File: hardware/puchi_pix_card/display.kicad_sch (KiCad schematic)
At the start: 286 parts, among them Q101 AO3401A, Q102 AO3401A, Q103 AO3401A, Q104 AO3401A, Q105 AO3401A, Q106 AO3401A, Q107 AO3401A, Q108 AO3401A, Q109 AO3401A, Q110 AO3401A, Q111 AO3401A, Q112 AO3401A, Q113 AO3401A, Q114 AO3401A, Q115 AO3401A, Q116 AO3401A, U101 MBI5153GP (R), U102 MBI5153GP (G), U103 MBI5153GP (B), U104 74HCT595, U105 74HCT595

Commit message: Fix design-review findings: I2C/PFET-gate pull-ups, red-column VDROP, D1/L1 part selection, USB-C 16P, USB power policy, MBI GCLK dead time and sleep leak paths
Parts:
- added R105, R106, R107, R108, R109, R110, R111, R112, R113, R114, R115, R116, R117, R118, R119, R120: 180, Resistor_SMD:R_0402_1005Metric, symbol Device:R
- added R121, R122, R123, R124, R125, R126, R127, R128, R129, R130, R131, R132, R133, R134, R135, R136: 100k, Resistor_SMD:R_0402_1005Metric, symbol Device:R
- R101: value 1.5k -> 1.8k
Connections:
- net +5V: now also R121.1, R122.1, R123.1, R124.1, R125.1, R126.1, R127.1, R128.1, R129.1, R130.1, R131.1, R132.1, R133.1, R134.1, R135.1, R136.1
- net COL_R0: now also R105.2; no longer U101.5 (OUT0)
- net COL_R1: now also R106.2; no longer U101.6 (OUT1)
- net COL_R10: now also R115.2; no longer U101.15 (OUT10)
- net COL_R11: now also R116.2; no longer U101.16 (OUT11)
- net COL_R12: now also R117.2; no longer U101.17 (OUT12)
- net COL_R13: now also R118.2; no longer U101.18 (OUT13)
- net COL_R14: now also R119.2; no longer U101.19 (OUT14)
- net COL_R15: now also R120.2; no longer U101.20 (OUT15)
- net COL_R2: now also R107.2; no longer U101.7 (OUT2)
- net COL_R3: now also R108.2; no longer U101.8 (OUT3)
- net COL_R4: now also R109.2; no longer U101.9 (OUT4)
- net COL_R5: now also R110.2; no longer U101.10 (OUT5)
- net COL_R6: now also R111.2; no longer U101.11 (OUT6)
- net COL_R7: now also R112.2; no longer U101.12 (OUT7)
- net COL_R8: now also R113.2; no longer U101.13 (OUT8)
- net COL_R9: now also R114.2; no longer U101.14 (OUT9)
- net SR_Q0: now also R121.2
- net SR_Q1: now also R122.2
- net SR_Q10: now also R131.2
- net SR_Q11: now also R132.2
- net SR_Q12: now also R133.2
- net SR_Q13: now also R134.2
- net SR_Q14: now also R135.2
- net SR_Q15: now also R136.2
- net SR_Q2: now also R123.2
- net SR_Q3: now also R124.2
- net SR_Q4: now also R125.2
- net SR_Q5: now also R126.2
- net SR_Q6: now also R127.2
- net SR_Q7: now also R128.2
- net SR_Q8: now also R129.2
- net SR_Q9: now also R130.2
- new net: R105.1, U101.5 (OUT0)
- new net: R108.1, U101.8 (OUT3)
- new net: R120.1, U101.20 (OUT15)
- new net: R113.1, U101.13 (OUT8)
- new net: R109.1, U101.9 (OUT4)
- new net: R117.1, U101.17 (OUT12)
- new net: R110.1, U101.10 (OUT5)
- new net: R114.1, U101.14 (OUT9)
- new net: R111.1, U101.11 (OUT6)
- new net: R112.1, U101.12 (OUT7)
- new net: R115.1, U101.15 (OUT10)
- new net: R116.1, U101.16 (OUT11)
- new net: R118.1, U101.18 (OUT13)
- new net: R119.1, U101.19 (OUT14)
- new net: R106.1, U101.6 (OUT1)
- new net: R107.1, U101.7 (OUT2)
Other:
- note added: "Rext: IOUT=(0.61V/Rext)x24 (MBI5153 p21) -> R 1.8k=8.1mA (+180R series drop, MBI DS p24), G 2.4k=6.1mA, B 4.7k=3.1mA max; config gain 12.5-200%."
- note removed: "Rext: IOUT=(0.61V/Rext)x24 (MBI5153 p21) -> R 1.5k=9.8mA, G 2.4k=6.1mA, B 4.7k=3.1mA max; config gain 12.5-200%."

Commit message: Fill LCSC part numbers for JLCPCB assembly; switch the column drivers to MBI5124GP-B (pin 21 GCLK -> /OE, net MBI_OE); R2 133k, in-stock LED/NOR listings
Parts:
- C101, C102, C103, C104, C105: LCSC (none) -> C309458
- D101, D102, D103, D104, D105, D106, D107, D108, D109, D110, D111, D112, D113, D114, D115, D116, D117, D118, D119, D120, D121, D122, D123, D124, D125, D126, D127, D128, D129, D130, D131, D132, D133, D134, D135, D136, D137, D138, D139, D140, D141, D142, D143, D144, D145, D146, D147, D148, D149, D150, D151, D152, D153, D154, D155, D156, D157, D158, D159, D160, D161, D162, D163, D164, D165, D166, D167, D168, D169, D170, D171, D172, D173, D174, D175, D176, D177, D178, D179, D180, D181, D182, D183, D184, D185, D186, D187, D188, D189, D190, D191, D192, D193, D194, D195, D196, D197, D198, D199, D200, D201, D202, D203, D204, D205, D206, D207, D208, D209, D210, D211, D212, D213, D214, D215, D216, D217, D218, D219, D220, D221, D222, D223, D224, D225, D226, D227, D228, D229, D230, D231, D232, D233, D234, D235, D236, D237, D238, D239, D240, D241, D242, D243, D244, D245, D246, D247, D248, D249, D250, D251, D252, D253, D254, D255, D256, D257, D258, D259, D260, D261, D262, D263, D264, D265, D266, D267, D268, D269, D270, D271, D272, D273, D274, D275, D276, D277, D278, D279, D280, D281, D282, D283, D284, D285, D286, D287, D288, D289, D290, D291, D292, D293, D294, D295, D296, D297, D298, D299, D300, D301, D302, D303, D304, D305, D306, D307, D308, D309, D310, D311, D312, D313, D314, D315, D316, D317, D318, D319, D320, D321, D322, D323, D324, D325, D326, D327, D328, D329, D330, D331, D332, D333, D334, D335, D336, D337, D338, D339, D340, D341, D342, D343, D344, D345, D346, D347, D348, D349, D350, D351, D352, D353, D354, D355, D356: LCSC C108793 -> C42421005
- Q101, Q102, Q103, Q104, Q105, Q106, Q107, Q108, Q109, Q110, Q111, Q112, Q113, Q114, Q115, Q116: LCSC (none) -> C15127
- R101: LCSC (none) -> C25871
- R102: LCSC (none) -> C25882
- R103: LCSC (none) -> C25900
- R104: LCSC (none) -> C25744
- R105, R106, R107, R108, R109, R110, R111, R112, R113, R114, R115, R116, R117, R118, R119, R120: LCSC (none) -> C38941
- R121, R122, R123, R124, R125, R126, R127, R128, R129, R130, R131, R132, R133, R134, R135, R136: LCSC (none) -> C25741
- U101: value MBI5153GP (R) -> MBI5124GP-B (R); symbol puchi_pix_card:MBI5153GP -> puchi_pix_card:MBI5124GP; LCSC C183654 -> C256866
- U102: value MBI5153GP (G) -> MBI5124GP-B (G); symbol puchi_pix_card:MBI5153GP -> puchi_pix_card:MBI5124GP; LCSC C183654 -> C256866
- U103: value MBI5153GP (B) -> MBI5124GP-B (B); symbol puchi_pix_card:MBI5153GP -> puchi_pix_card:MBI5124GP; LCSC C183654 -> C256866
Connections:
- net GCLK renamed MBI_OE

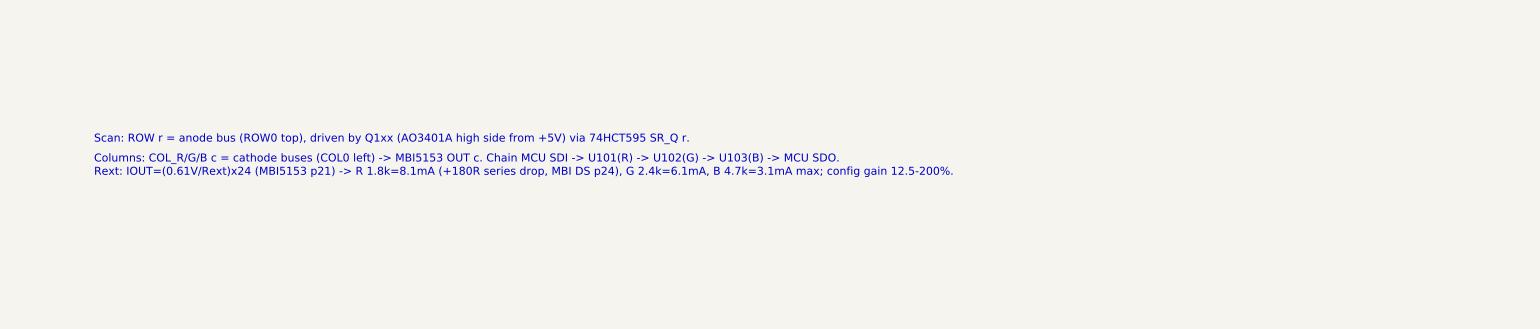
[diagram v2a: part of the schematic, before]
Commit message: Review fixes: guard the first plane against ISR re-entry, SPI2 8 MHz for the 3.3V chain delay, release the KXTJ3 latched INT, force /OE high on stop; J2 real part name and footprint id; drop MBI5153 leftovers
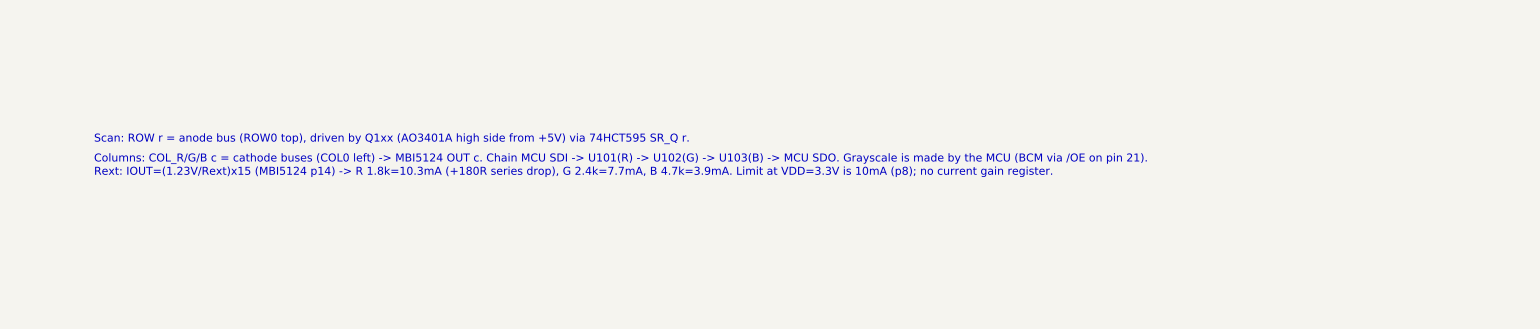
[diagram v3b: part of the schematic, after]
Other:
- note added: "Columns: COL_R/G/B c = cathode buses (COL0 left) -> MBI5124 OUT c. Chain MCU SDI -> U101(R) -> U102(G) -> U103(B) -> MCU SDO. Grayscale is made by the MCU (BCM via /OE on pin 21)."
- note added: "Rext: IOUT=(1.23V/Rext)x15 (MBI5124 p14) -> R 1.8k=10.3mA (+180R series drop), G 2.4k=7.7mA, B 4.7k=3.9mA. Limit at VDD=3.3V is 10mA (p8); no current gain register."
- note removed: "Columns: COL_R/G/B c = cathode buses (COL0 left) -> MBI5153 OUT c. Chain MCU SDI -> U101(R) -> U102(G) -> U103(B) -> MCU SDO."
- note removed: "Rext: IOUT=(0.61V/Rext)x24 (MBI5153 p21) -> R 1.8k=8.1mA (+180R series drop, MBI DS p24), G 2.4k=6.1mA, B 4.7k=3.1mA max; config gain 12.5-200%."
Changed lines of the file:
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@@
 		)
 	)
-	(text "Columns: COL_R/G/B c = cathode buses (COL0 left) -> MBI5153 OUT c. Chain MCU SDI -> U101(R) -> U102(G) -> U103(B) -> MCU SDO."
+	(text "Columns: COL_R/G/B c = cathode buses (COL0 left) -> MBI5124 OUT c. Chain MCU SDI -> U101(R) -> U102(G) -> U103(B) -> MCU SDO. Grayscale is made by the MCU (BCM via /OE on pin 21)."
 		(exclude_from_sim no)
 		(at 299.72 303.53 0)
@@
 		)
 	)
-	(text "Rext: IOUT=(0.61V/Rext)x24 (MBI5153 p21) -> R 1.8k=8.1mA (+180R series drop, MBI DS p24), G 2.4k=6.1mA, B 4.7k=3.1mA max; config gain 12.5-200%."
+	(text "Rext: IOUT=(1.23V/Rext)x15 (MBI5124 p14) -> R 1.8k=10.3mA (+180R series drop), G 2.4k=7.7mA, B 4.7k=3.9mA. Limit at VDD=3.3V is 10mA (p8); no current gain register."
 		(exclude_from_sim no)
 		(at 299.72 306.07 0)

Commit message: Move SW1 into the +3V3S branch (boost VIN on VBAT) so the 0.1A switch carries only the MCU rail; R101 2.0k / red series 120R for the MBI5124 10mA limit and USB headroom; R9 4.7k; C1 next to U1; In1 GND plane rejoined
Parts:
- R101: value 1.8k -> 2.0k; LCSC C25871 -> C4109
- R105, R106, R107, R108, R109, R110, R111, R112, R113, R114, R115, R116, R117, R118, R119, R120: value 180 -> 120; LCSC C38941 -> C25079
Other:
- note added: "Rext: IOUT=(1.23V/Rext)x15 (MBI5124 p14) -> R 2.0k=9.2mA (+120R series drop), G 2.4k=7.7mA, B 4.7k=3.9mA. Limit at VDD=3.3V is 10mA (p8); no current gain register. Red series 120R: on USB (+5V >= 4.0V after D1) worst-case red VF 2.4V + 1.11V + VDS 0.5V = 4.0V."
- note removed: "Rext: IOUT=(1.23V/Rext)x15 (MBI5124 p14) -> R 1.8k=10.3mA (+180R series drop), G 2.4k=7.7mA, B 4.7k=3.9mA. Limit at VDD=3.3V is 10mA (p8); no current gain register."

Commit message: Add C106 10uF bulk capacitor on +5V next to the row PFET column (row switching transient, USB headroom)
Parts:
- added C106: 10uF, Capacitor_SMD:C_0603_1608Metric, symbol Device:C
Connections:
- net +5V: now also C106.1
- net GND: now also C106.2
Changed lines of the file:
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@@
 	(wire
 		(pts
+			(xy 474.98 109.22) (xy 474.98 106.68)
+		)
+		(stroke
+			(width 0)
+			(type default)
+		)
+	)
+	(global_label "+5V"
+		(shape input)
+		(at 474.98 106.68 90)
+		(effects
+			(font
+				(size 1.27 1.27)
+			)
+			(justify left)
+		)
+		(property "Intersheetrefs" "${INTERSHEET_REFS}"
+			(at 535.94 157.48 0)
+			(effects
+				(font
+					(size 1.27 1.27)
+				)
+				(hide yes)
+			)
+		)
+	)
+	(wire
+		(pts
 			(xy 269.24 95.25) (xy 269.24 97.79)
 		)
@@
 					(unit 1)
 				)
+			)
+		)
+	)
+	(symbol
+		(lib_id "Device:C")
+		(at 474.98 113.03 0)
+		(unit 1)
+		(exclude_from_sim no)
+		(in_bom yes)
+		(on_board yes)
+		(dnp no)
+		(property "Reference" "C106"
+			(at 477.52 111.76 0)
+			(effects
+				(font
+					(size 1.27 1.27)
+				)
+				(justify left)
+			)
+		)
+		(property "Value" "10uF"
+			(at 477.52 114.3 0)
+			(effects
+				(font
+					(size 1.016 1.016)
+				)
+				(justify left)
+			)
+		)
+		(property "Footprint" "Capacitor_SMD:C_0603_1608Metric"
+			(at 474.98 113.03 0)
+			(effects
+				(font
+					(size 1.27 1.27)
+				)
+				(hide yes)
+			)
+		)
+		(property "Datasheet" ""
+			(at 474.98 113.03 0)
+			(effects
+				(font
+					(size 1.27 1.27)
+				)
+				(hide yes)
+			)
+		)
+		(property "Description" ""
+			(at 474.98 113.03 0)
+			(effects
+				(font
+					(size 1.27 1.27)
+				)
+			)
+		)
+		(property "LCSC" "C96446"
+			(at 474.98 113.03 0)
+			(effects
+				(font
+					(size 1.27 1.27)
+				)
+				(hide yes)
+			)
+		)
+		(pin "1"
+		)
+		(pin "2"
+		)
+		(instances
+			(project "puchi_pix_card"
+				(path "/68e11f83-6621-4a95-99d2-cf3319172deb/39b95bc8-43d3-4bee-847f-f27193d97409"
+					(reference "C106")
+					(unit 1)
+				)
+			)
+		)
+	)
+	(symbol
+		(lib_id "power:GND")
+		(at 474.98 116.84 0)
+		(unit 1)
+		(exclude_from_sim no)
+		(in_bom yes)
+		(on_board yes)
+		(dnp no)
+		(property "Reference" "#PWR114"
+			(at 474.98 116.84 0)
+			(effects
+				(font
+					(size 1.27 1.27)
+				)
+				(justify left)
+			)
+		)
+		(property "Value" "GND"
+			(at 474.98 120.65 0)
+			(effects
+				(font
+					(size 1.016 1.016)
+				)
+				(justify left)
+			)
+		)
+		(property "Footprint" ""
+			(at 474.98 116.84 0)
+			(effects
+				(font
+					(size 1.27 1.27)
+				)
+				(hide yes)
+			)
+		)
+		(property "Datasheet" ""
+			(at 474.98 116.84 0)
+			(effects
+				(font
+					(size 1.27 1.27)
+				)
+				(hide yes)
+			)
+		)
+		(property "Description" ""
+			(at 474.98 116.84 0)
+			(effects
+				(font
+					(size 1.27 1.27)
+				)
+			)
+		)
+		(pin "1"
+		)
+		(instances
+			(project "puchi_pix_card"
+				(path "/68e11f83-6621-4a95-99d2-cf3319172deb/39b95bc8-43d3-4bee-847f-f27193d97409"
+					(reference "#PWR114")
+					(unit 1)
+				)
